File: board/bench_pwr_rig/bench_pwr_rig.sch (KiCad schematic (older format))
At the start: 4 parts

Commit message: Use photon
Updated schematic to use particle photon device for 3.3V interface to existing NHD-0208AZ-RN-YBW-3V in stock
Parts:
- removed A?: Arduino_UNO_R2, Module:Arduino_UNO_R2, symbol MCU_Module:Arduino_UNO_R2
- added R?: R, symbol Device:R
- added RV?: R_POT_TRIM, symbol Device:R_POT_TRIM
- added U?: PHOTON, symbol MCU_Module:PHOTON
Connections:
- wire segments 29 -> 37
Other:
- moved on the sheet: Q?, U?

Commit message: Updated powertrain schematic
Changed powertrain to PSFB
Updated schematic
Added new symbols
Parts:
- RV?: symbol Device:R_POT_TRIM -> bench_pwr_rig-rescue:R_POT_TRIM-Device
- U?: symbol MCU_Module:PHOTON -> bench_pwr_rig-rescue:PHOTON-MCU_Module
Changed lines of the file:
@@
 EESchema Schematic File Version 4
+LIBS:bench_pwr_rig-cache
 EELAYER 29 0
 EELAYER END
@@
 S 8500 1700 1100 500
 U 5F8A85F6
-F0 "buck_boost" 50
-F1 "buck_boost.sch" 50
+F0 "PSFB" 50
+F1 "PSFB.sch" 50
+F2 "VCTL" I R 9600 2000 50
+F3 "ICTL" I R 9600 2100 50
+F4 "OUTP" U R 9600 1750 50
+F5 "OUTN" U R 9600 1850 50
+F6 "VINP" U L 8500 1750 50
+F7 "VINN" U L 8500 1850 50
 $EndSheet
 NoConn ~ 3350 2000
@@
 $EndComp
 $Comp
-L MCU_Module:PHOTON U?
+L bench_pwr_rig-rescue:PHOTON-MCU_Module U?
 U 1 1 5F8C1D8A
 P 1950 2500
@@
 	4150 2000 4150 2100
 $Comp
-L Device:R_POT_TRIM RV?
+L bench_pwr_rig-rescue:R_POT_TRIM-Device RV?
 U 1 1 5F8D3240
 P 4450 3150

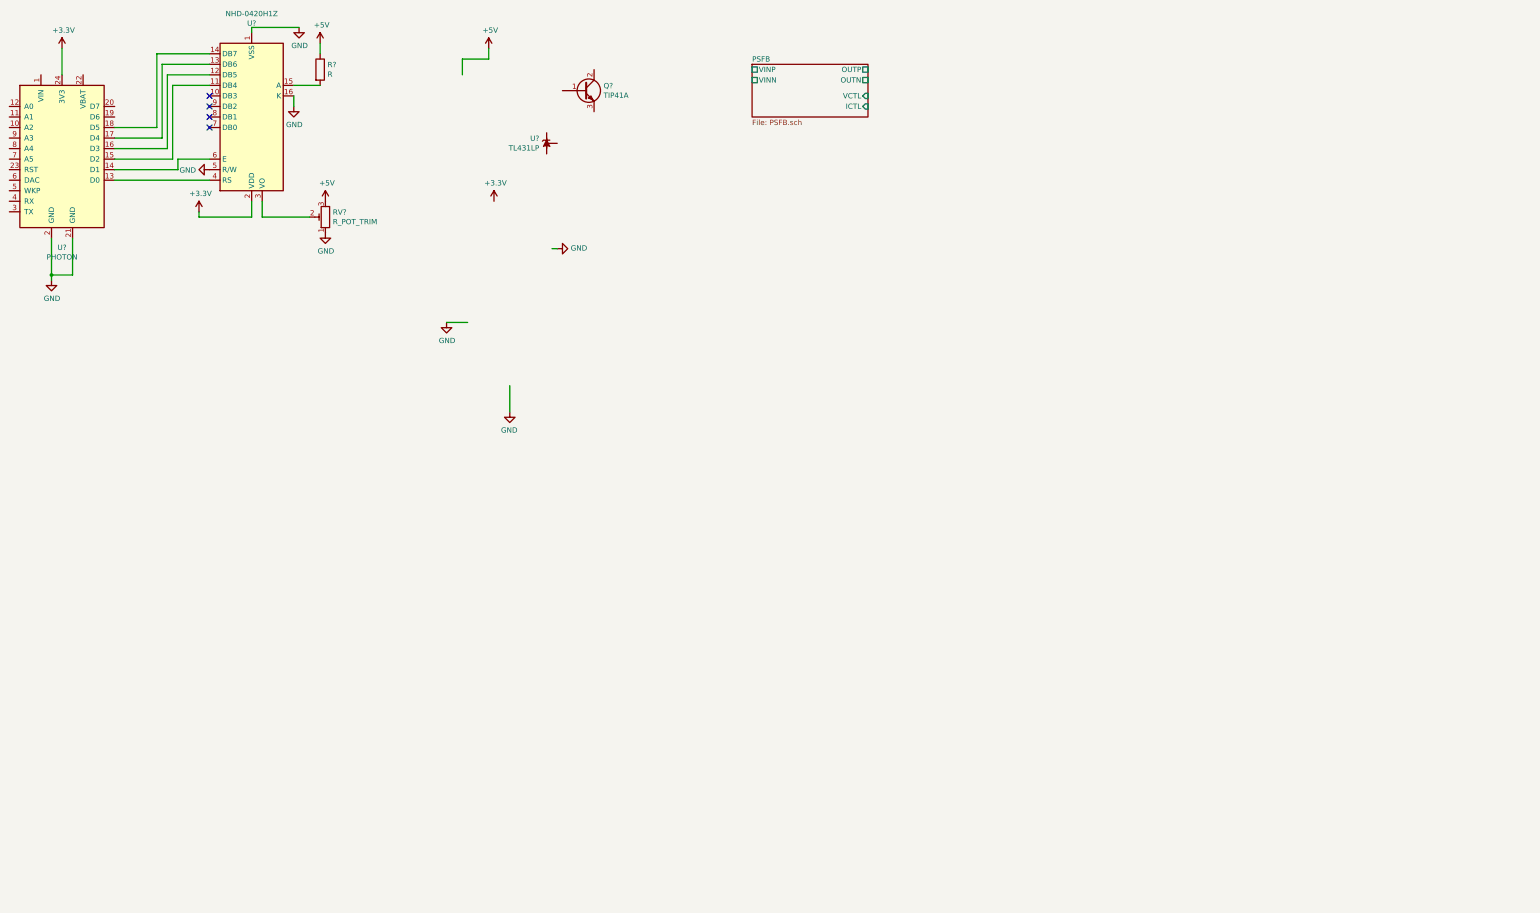
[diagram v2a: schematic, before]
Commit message: Schematic Update
Updated schematic
Added Input Filter and PFC sections
Added capacitor, resistor, and protection parts library
Started a jupyter notebook for PFC section
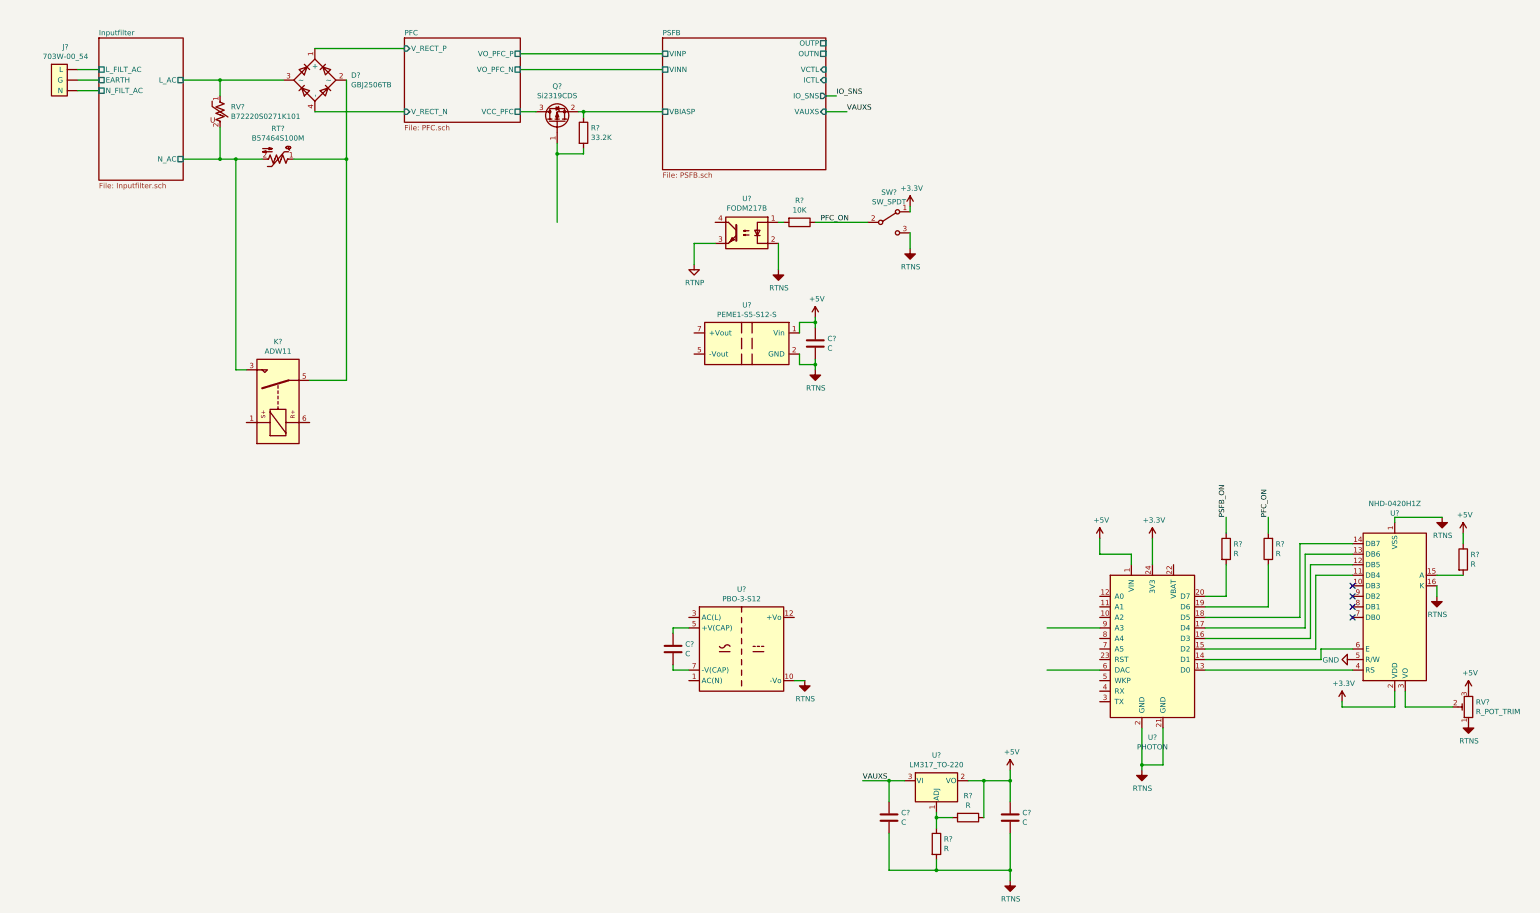
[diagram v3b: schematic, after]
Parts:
- removed Q?: TIP41A, Package_TO_SOT_THT:TO-220-3_Vertical, symbol Transistor_BJT:TIP41A
- removed U?: TL431LP, Package_TO_SOT_THT:TO-92_Inline, symbol Reference_Voltage:TL431LP
- added C? (x4): C, symbol Device:C
- added D?: GBJ2506TB, Diode_THT:Diode_Bridge_30.0x4.6x20.0mm_P10.0mm_P7.5mm, symbol Diode_Bridge:GBJ2506TB
- added J?: 703W-00_54, Connector:703W-00, symbol Connector:703W-00_54
- added K?: ADW11, Relay_THT:Relay_1P1T_NO_10x24x18.8mm_Panasonic_ADW11xxxxW_THT, symbol Relay:ADW11
- added Q?: Si2319CDS, Package_TO_SOT_SMD:SOT-23, symbol Transistor_FET:Si2319CDS
- added R? (x4): R, symbol Device:R
- added R?: CRCW060333K2FKEA, Resistor_SMD:R_0603_1608Metric_Pad1.05x0.95mm_HandSolder, symbol Resistor:CRCW060333K2FKEA
- added R?: CRCW060310K0FKEA, Resistor_SMD:R_0603_1608Metric_Pad1.05x0.95mm_HandSolder, symbol Resistor:CRCW060310K0FKEA
- added RT?: B57464S100M, Capacitor_THT:C_Disc_D16.0mm_W5.0mm_P7.50mm, symbol Resistor:B57464S100M
- added RV?: B72220S0271K101, Capacitor_THT:C_Disc_D16.0mm_W5.0mm_P10.00mm, symbol Protection:B72220S0271K101
- added SW?: SW_SPDT, symbol Switch:SW_SPDT
- added U?: PBO-3-S12, Converter_ACDC:Converter_ACDC_CUI_PBO-3-Sxx_THT_Vertical, symbol Converter_ACDC:PBO-3-S12
- added U?: FODM217B, Package_SO:SOP-4_4.4x2.6mm_P1.27mm, symbol Isolator:FODM217B
- added U?: PEME1-S5-S12-S, symbol Converter_DCDC:PEME1-S5-S12-S
- added U?: LM317_TO-220, Package_TO_SOT_THT:TO-220-3_Vertical, symbol Regulator_Linear:LM317_TO-220
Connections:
- net labels added: IO_SNS, PFC_ON, PSFB_ON, RTNP, RTNS, VAUXS
- wire segments 37 -> 109
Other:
- moved on the sheet: R?, RV?, U?

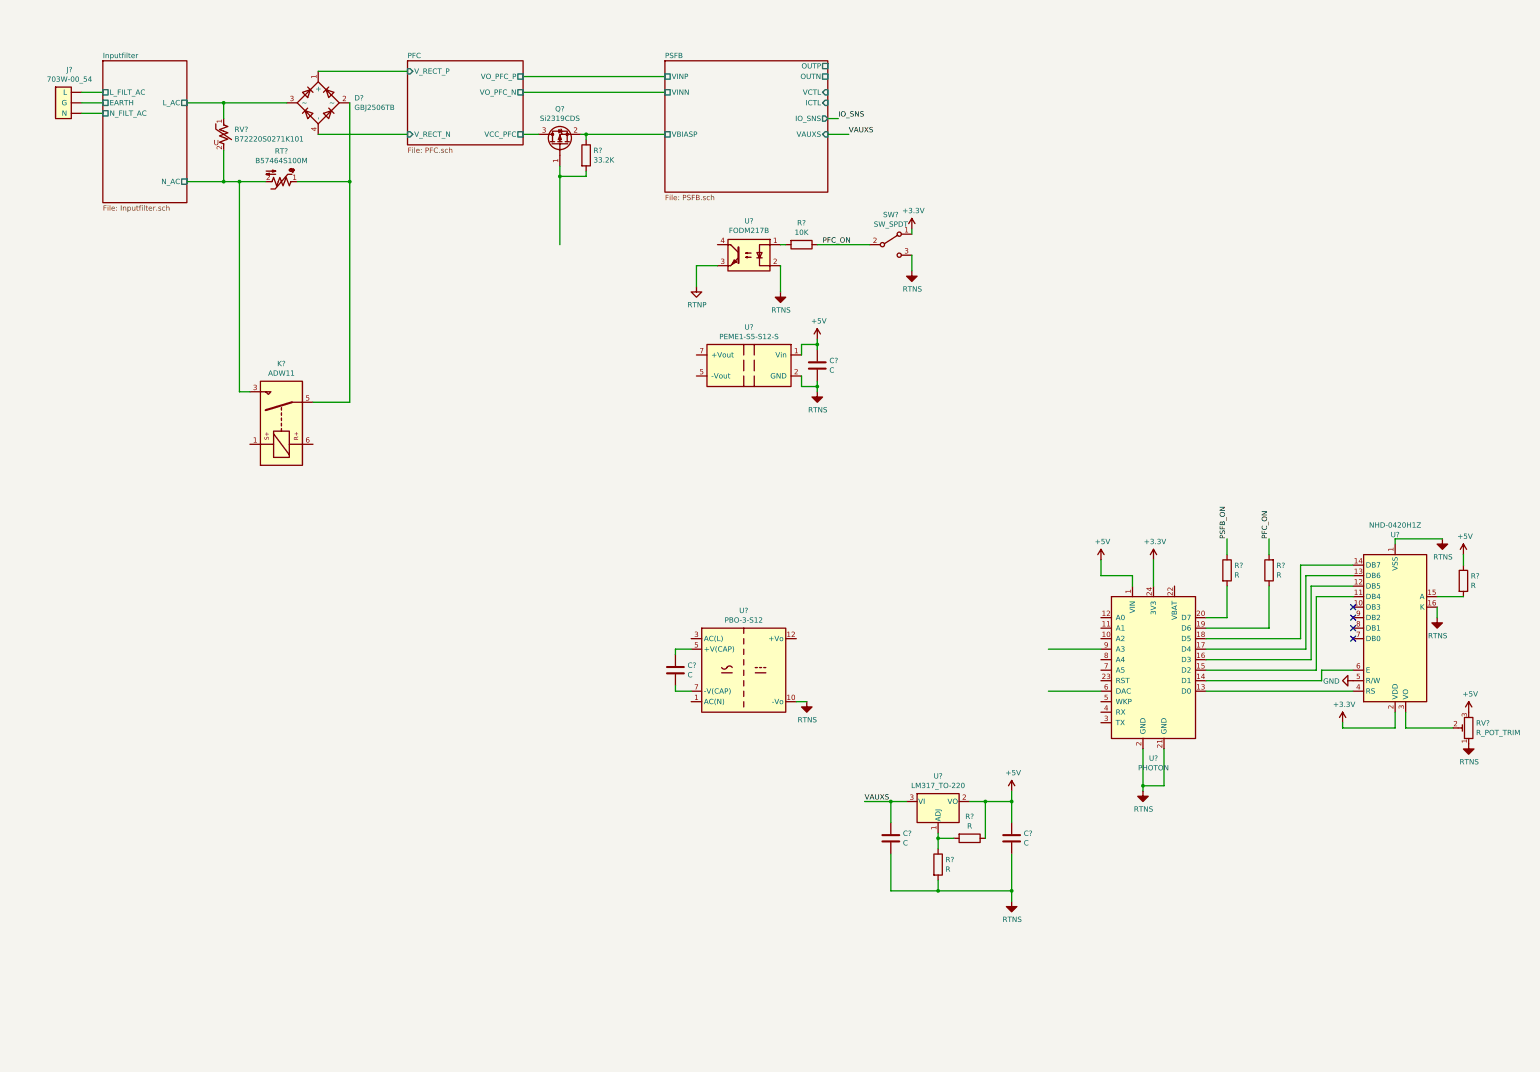
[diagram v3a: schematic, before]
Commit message: schematic and layout updates
Finalized schematic for rev 0.1. Anticipate additional component values update through analysis. Moving to layout
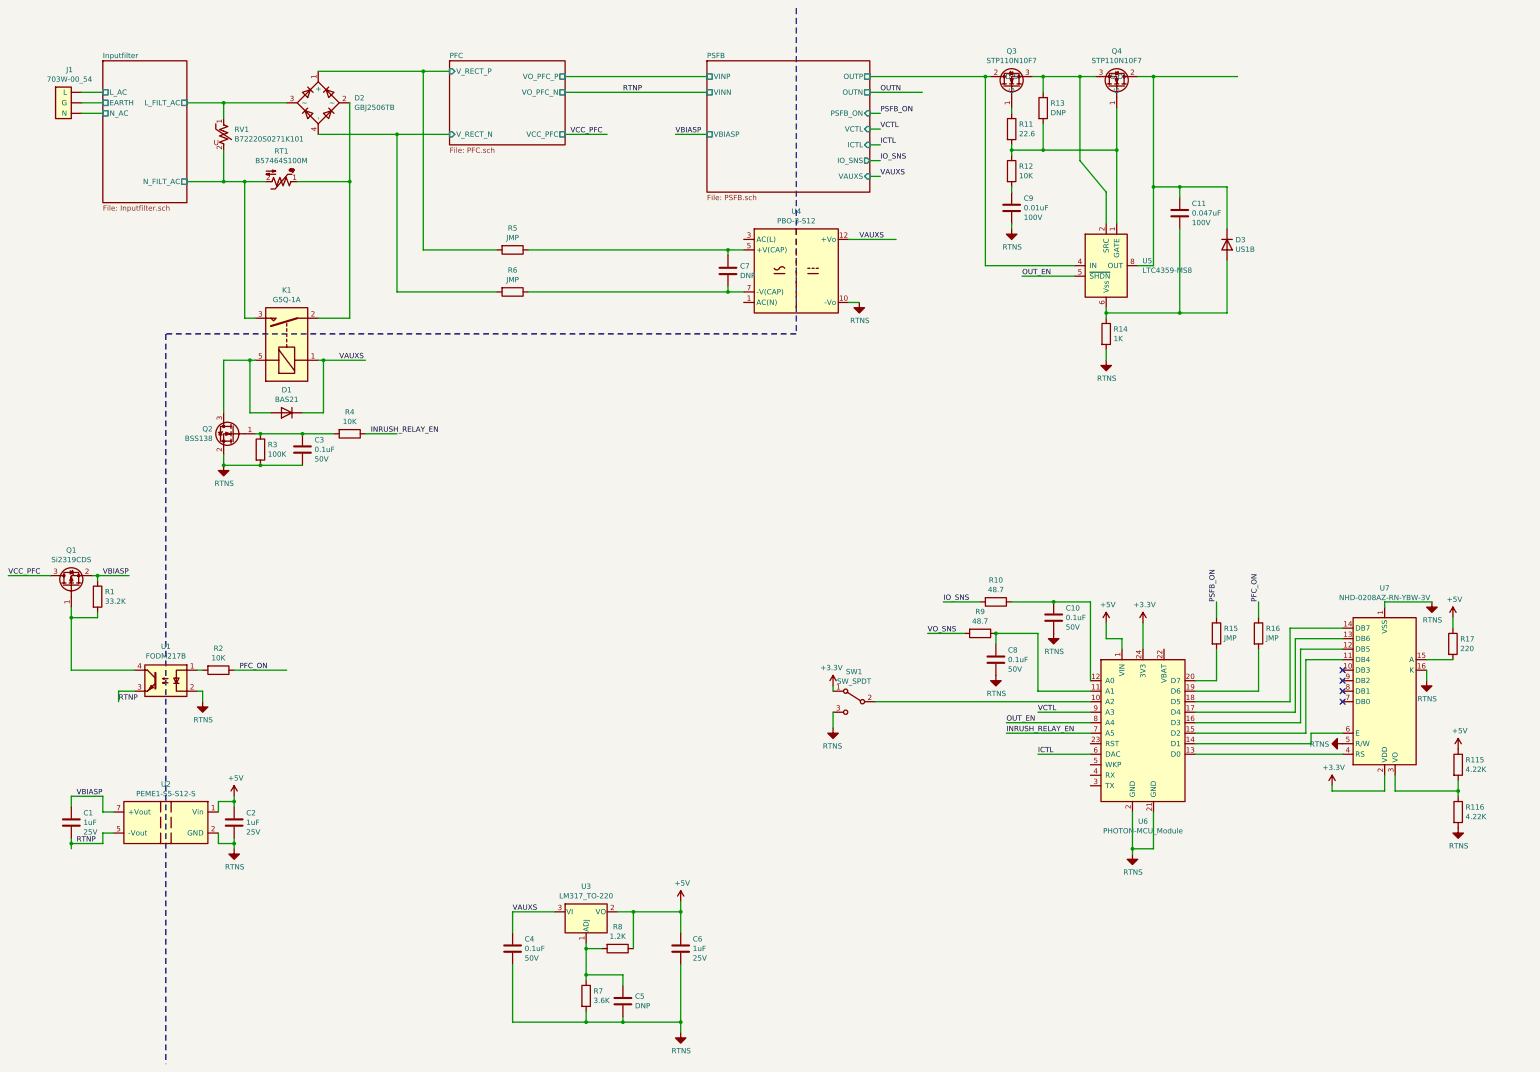
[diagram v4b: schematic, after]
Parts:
- removed C? (x3): C, symbol Device:C
- removed K?: ADW11, Relay_THT:Relay_1P1T_NO_10x24x18.8mm_Panasonic_ADW11xxxxW_THT, symbol Relay:ADW11
- removed R? (x5): R, symbol Device:R
- removed RV?: R_POT_TRIM, symbol bench_pwr_rig-rescue:R_POT_TRIM-Device
- removed U?: NHD-0420H1Z, Display:NHD-0420H1Z, symbol Display_Character:NHD-0420H1Z
- removed U?: PHOTON, symbol bench_pwr_rig-rescue:PHOTON-MCU_Module
- added C1, C2, C6: C1608X7R1E105K080AB, Capacitor_SMD:C_0603_1608Metric_Pad1.05x0.95mm_HandSolder, symbol Capacitor:C1608X7R1E105K080AB
- added C10, C3, C4, C8: C1608X7R1H104K, Capacitor_SMD:C_0603_1608Metric_Pad1.05x0.95mm_HandSolder, symbol Capacitor:C1608X7R1H104K
- added C11: CL21B473KCFNNNE, Capacitor_SMD:C_0805_2012Metric_Pad1.15x1.40mm_HandSolder, symbol Capacitor:CL21B473KCFNNNE
- added C5: DNP, Capacitor_SMD:C_0603_1608Metric_Pad1.05x0.95mm_HandSolder, symbol Capacitor:DNP
- added C9: CL21B103KCANNNC, Capacitor_SMD:C_0805_2012Metric_Pad1.15x1.40mm_HandSolder, symbol Capacitor:CL21B103KCANNNC
- added D1: BAS21, Package_TO_SOT_SMD:SOT-23, symbol Diode:BAS21
- added D3: US1B, Diode_SMD:D_SMA, symbol Diode:US1B
- added K1: G5Q-1A, Relay_THT:Relay_SPST_Omron-G5Q-1A, symbol Relay:G5Q-1A
- added Q2: BSS138, Package_TO_SOT_SMD:SOT-23, symbol Transistor_FET:BSS138
- added Q3, Q4: STP110N10F7, Package_TO_SOT_THT:TO-220-3_Vertical, symbol Transistor_FET:STP110N10F7
- added R10, R9: 0603WAF4872T5E, Resistor_SMD:R_0603_1608Metric_Pad1.05x0.95mm_HandSolder, symbol Resistor:0603WAF4872T5E
- added R11: 0603WAF226JT5E, Resistor_SMD:R_0603_1608Metric_Pad1.05x0.95mm_HandSolder, symbol Resistor:0603WAF226JT5E
- added R115, R116: 0603WAF4221T5E, Resistor_SMD:R_0603_1608Metric_Pad1.05x0.95mm_HandSolder, symbol Resistor:0603WAF4221T5E
- added R12, R4: CRCW060310K0FKEA, Resistor_SMD:R_0603_1608Metric_Pad1.05x0.95mm_HandSolder, symbol Resistor:CRCW060310K0FKEA
- added R13: DNP, Resistor_SMD:R_0603_1608Metric_Pad1.05x0.95mm_HandSolder, symbol Resistor:DNP
- added R14: 0805W8F1001T5E, Resistor_SMD:R_0805_2012Metric_Pad1.15x1.40mm_HandSolder, symbol Resistor:0805W8F1001T5E
- added R15, R16, R5, R6: JMP, Resistor_SMD:R_0603_1608Metric_Pad1.05x0.95mm_HandSolder, symbol Resistor:JMP
- added R17: 0603WAF2200T5E, Resistor_SMD:R_0603_1608Metric_Pad1.05x0.95mm_HandSolder, symbol Resistor:0603WAF2200T5E
- added R3: 0603WAF1003T5E, Resistor_SMD:R_0603_1608Metric_Pad1.05x0.95mm_HandSolder, symbol Resistor:0603WAF1003T5E
- added R7: 0603WAF3601T5E, Resistor_SMD:R_0603_1608Metric_Pad1.05x0.95mm_HandSolder, symbol Resistor:0603WAF3601T5E
- added R8: 0603WAF1201T5E, Resistor_SMD:R_0603_1608Metric_Pad1.05x0.95mm_HandSolder, symbol Resistor:0603WAF1201T5E
- added U5: LTC4359-MS8, Package_SO:MSOP-8_3x3mm_P0.65mm, symbol Power_Management:LTC4359-MS8
- added U6: PHOTON-MCU_Module, RF_Module:photon_tht, symbol RF_Module:PHOTON-MCU_Module
- added U7: NHD-0208AZ-RN-YBW-3V, Connector_PinHeader_2.54mm:PinHeader_2x08_P2.54mm_Vertical, symbol Display_Character:NHD-0208AZ-RN-YBW-3V
- C7: renamed from C?; value C -> DNP; footprint (none) -> Capacitor_SMD:C_1206_3216Metric
- SW1: renamed from SW?; footprint (none) -> Button_Switch_SMD:SW_SPDT_CK-JS102011SAQN
- U2: renamed from U?; footprint (none) -> Converter_DCDC:Converter_DCDC_Murata_MGJ2DxxxxxxSC_THT
- gave numbers to parts that had none: 10
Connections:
- net labels added: ICTL, INRUSH_RELAY_EN, OUTN, OUT_EN, VBIASP, VCC_PFC, VCTL, VO_SNS
- net labels removed: GND
- wire segments 109 -> 207
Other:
- moved on the sheet: C7, Q1, R1, R2, SW1, U1, U2, U3, U4
